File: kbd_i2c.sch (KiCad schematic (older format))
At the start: 78 parts, among them J1 Conn_01x04, SW1 MX_1u, SW10 MX_1u, SW11 MX_1u, SW12 MX_1u, SW13 MX_1u, SW14 MX_1u, SW15 MX_1u, SW16 MX_1u, SW17 MX_1u, SW18 MX_1u, SW19 MX_1u, SW2 MX_1u, SW20 MX_1u, SW21 MX_1u, SW22 MX_1u, SW23 MX_1u, SW24 MX_1u, SW25 SW_Push, SW26 SW_Push, SW27 SW_Push, SW28 SW_Push, SW3 MX_1u, SW4 MX_1u, SW5 MX_1u, SW6 MX_1u, SW7 MX_1u, SW8 MX_1u, SW9 MX_1u, U1 MCP23017_SO

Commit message: correction empreinte et routage; utilisation empreinte cherry mx led
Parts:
- removed D25, D28, D29, D32: LED, LED_THT:LED_D5.0mm, symbol Device:LED
- removed SW11, SW17, SW24, SW5: MX_1u, Button_Switch_Keyboard:SW_Cherry_MX_1.00u_PCB, symbol Switch:SW_Push
- added SW11, SW17, SW23, SW5: SW_Push_LED, Chimere:SW_MX_LED, symbol Switch:SW_Push_LED
- renumbered D20 to D19, D21 to D20, D22 to D21, D23 to D22, D24 to D23, D19 to D24, SW20 to SW19, SW21 to SW20, SW22 to SW21, SW23 to SW22, SW19 to SW24
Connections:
- wire segments 205 -> 201
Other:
- moved on the sheet: D1, D10, D11, D12, D13, D14, D15, D16, D17, D18, D19, D2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

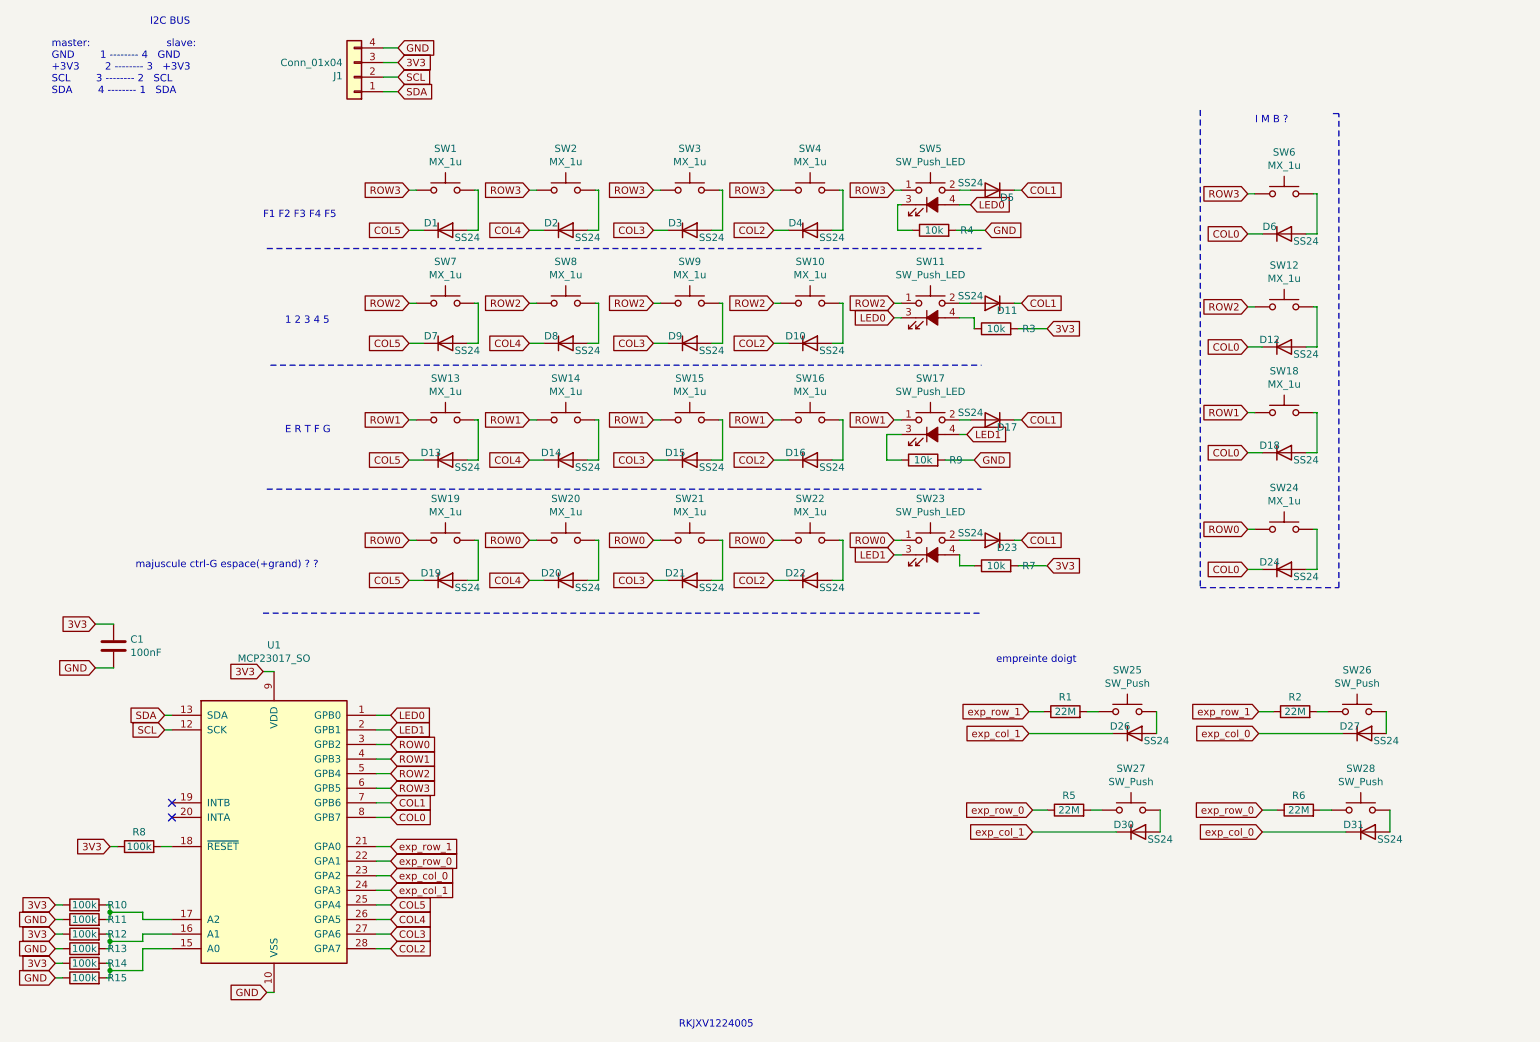
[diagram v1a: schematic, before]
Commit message: schema + routage
- redistribution des touches
- ajout 5ways switch
- supprimé les empreintes pcb de touches résistives
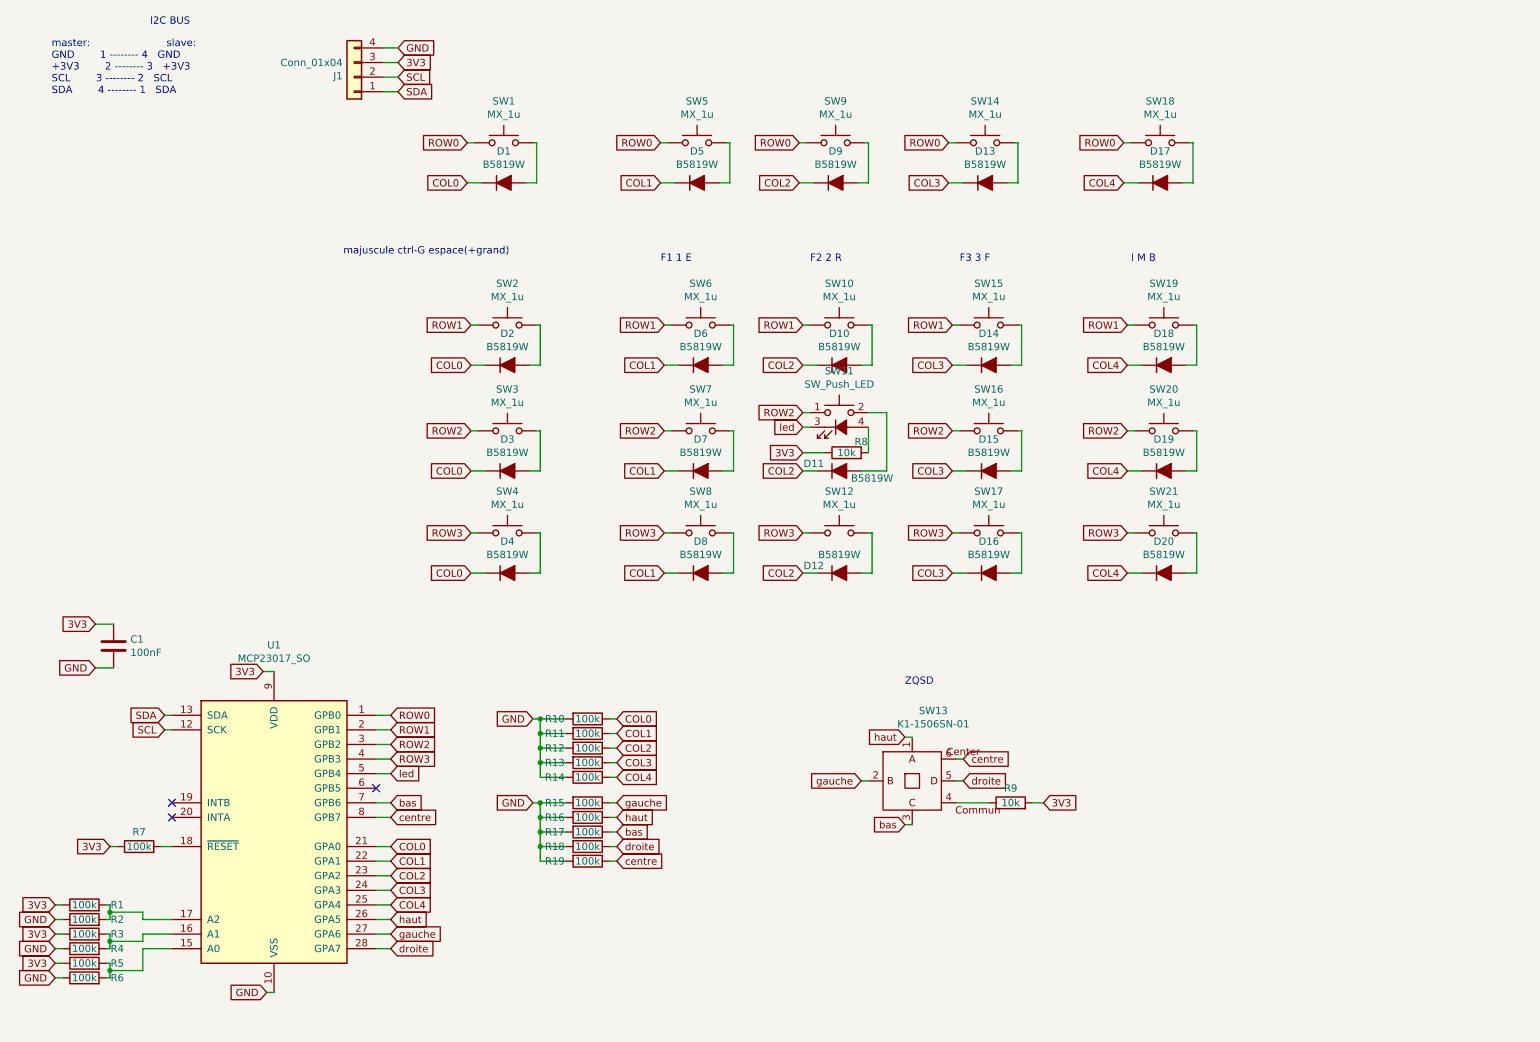
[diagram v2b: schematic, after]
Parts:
- removed D1, D10, D11, D12, D13, D14, D15, D16, D17, D18, D19, D2, D20, D21, D22, D23, D24, D26, D27, D3, D30, D31, D4, D5, D6, D7, D8, D9: SS24, Diode_SMD:D_SMA, symbol Device:D
- removed R1, R2, R5, R6: 22M, Resistor_SMD:R_0603_1608Metric_Pad1.05x0.95mm_HandSolder, symbol Device:R
- removed R3, R4, R7: 10k, Resistor_SMD:R_0603_1608Metric_Pad1.05x0.95mm_HandSolder, symbol Device:R
- removed SW13, SW2, SW22, SW24, SW3, SW4: MX_1u, Button_Switch_Keyboard:SW_Cherry_MX_1.00u_PCB, symbol Switch:SW_Push
- removed SW17, SW23, SW5: SW_Push_LED, Chimere:SW_MX_LED, symbol Switch:SW_Push_LED
- removed SW25, SW26, SW27, SW28: SW_Push, Chimere:doigt_sw, symbol Switch:SW_Push
- added D1, D10, D11, D12, D13, D14, D15, D16, D17, D18, D19, D2, D20, D3, D4, D5, D6, D7, D8, D9: B5819W, Diode_SMD:D_SOD-123, symbol Device:D_ALT
- added R10, R11, R12, R13, R14, R15, R16, R17, R18, R19: 100k, Resistor_SMD:R_0603_1608Metric, symbol Device:R
- added R8: 10k, Resistor_SMD:R_0603_1608Metric, symbol Device:R
- added SW12, SW17, SW18, SW5, SW6: MX_1u, Button_Switch_Keyboard:SW_Cherry_MX_1.00u_PCB, symbol Switch:SW_Push
- added SW13: K1-1506SN-01, Chimere:K1-1506SN-01, symbol Chimere:K1-1506SN-01
- C1: footprint Capacitor_SMD:C_0603_1608Metric_Pad1.05x0.95mm_HandSolder -> Capacitor_SMD:C_0603_1608Metric
- R1: renamed from R10; footprint Resistor_SMD:R_0603_1608Metric_Pad1.05x0.95mm_HandSolder -> Resistor_SMD:R_0603_1608Metric
- R2: renamed from R11; footprint Resistor_SMD:R_0603_1608Metric_Pad1.05x0.95mm_HandSolder -> Resistor_SMD:R_0603_1608Metric
- R3: renamed from R12; footprint Resistor_SMD:R_0603_1608Metric_Pad1.05x0.95mm_HandSolder -> Resistor_SMD:R_0603_1608Metric
- R4: renamed from R13; footprint Resistor_SMD:R_0603_1608Metric_Pad1.05x0.95mm_HandSolder -> Resistor_SMD:R_0603_1608Metric
- R5: renamed from R14; footprint Resistor_SMD:R_0603_1608Metric_Pad1.05x0.95mm_HandSolder -> Resistor_SMD:R_0603_1608Metric
- R6: renamed from R15; footprint Resistor_SMD:R_0603_1608Metric_Pad1.05x0.95mm_HandSolder -> Resistor_SMD:R_0603_1608Metric
- R7: renamed from R8; footprint Resistor_SMD:R_0603_1608Metric_Pad1.05x0.95mm_HandSolder -> Resistor_SMD:R_0603_1608Metric
- R9: footprint Resistor_SMD:R_0603_1608Metric_Pad1.05x0.95mm_HandSolder -> Resistor_SMD:R_0603_1608Metric
- renumbered SW12 to SW2, SW18 to SW3, SW6 to SW4
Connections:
- net COL5 is gone; now on net COL4: U1.25 (GPA4)
- net LED1 is gone; now on net ROW1: U1.2 (GPB1)
- net exp_col_0 is gone; now on net COL2: U1.23 (GPA2)
- net exp_col_1 is gone; now on net COL3: U1.24 (GPA3)
- net exp_row_0 is gone; now on net COL1: U1.22 (GPA1)
- net exp_row_1 is gone; now on net COL0: U1.21 (GPA0)
- net 3V3: now also R9.2, R8.1
- net COL0: now also D1.1 (K), D2.1 (K), D3.1 (K), D4.1 (K), R10.1; no longer U1.8 (GPB7)
- net COL1: now also D5.1 (K), D6.1 (K), D7.1 (K), D8.1 (K), R11.1; no longer U1.7 (GPB6)
- net COL2: now also D10.1 (K), D11.1 (K), D12.1 (K), D9.1 (K), R12.1; no longer U1.28 (GPA7)
- net COL3: now also D13.1 (K), D14.1 (K), D15.1 (K), D16.1 (K), R13.1; no longer U1.27 (GPA6)
- net COL4: now also D17.1 (K), D18.1 (K), D19.1 (K), D20.1 (K), R14.1; no longer U1.26 (GPA5)
- net GND: now also R10.2, R11.2, R12.2, R13.2, R14.2, R15.2, R16.2, R17.2, R18.2, R19.2; no longer R9.2
- net ROW0: now also SW1.1, SW14.1, SW9.1, U1.1 (GPB0), SW18.1, SW5.1; no longer SW19.1, SW20.1, SW21.1, U1.3 (GPB2)
- net ROW1: now also SW10.1, SW19.1, SW2.1, SW6.1; no longer SW14.1, SW16.1, SW3.1, U1.4 (GPB3)
- net ROW2: now also SW16.1, SW20.1, SW3.1, U1.3 (GPB2); no longer SW10.1, SW2.1, SW8.1, SW9.1, U1.5 (GPB4)
- net ROW3: now also SW21.1, SW8.1, U1.4 (GPB3), SW12.1, SW17.1; no longer SW1.1, U1.6 (GPB5)
- net at SW1.2: now also D1.2 (A)
- net at SW4.2: now also D4.2 (A)
- net at SW7.2: now also D7.2 (A)
- net at SW8.2: now also D8.2 (A)
- net at SW9.2: now also D9.2 (A)
- net at SW10.2: now also D10.2 (A)
- net at SW2.2: now also D2.2 (A)
- net at SW14.2: now also D13.2 (A)
- net at SW15.2: now also D14.2 (A)
- net at SW16.2: now also D15.2 (A)
- net at SW3.2: now also D3.2 (A)
- net at SW19.2: now also D18.2 (A)
- net at SW20.2: now also D19.2 (A)
- net at SW21.2: now also D20.2 (A)
- net at SW11.4 (A): now also R8.2
- net at R9.1: now also SW13.4
- net at SW11.2: now also D11.2 (A)
- net LED0 renamed led
- net led: now also U1.5 (GPB4); no longer U1.1 (GPB0)
- new net: D6.2 (A), SW6.2
- new net: D12.2 (A), SW12.2
- new net: D16.2 (A), SW17.2
- new net: D5.2 (A), SW5.2
- new net: D17.2 (A), SW18.2
- new net bas: R17.1, SW13.3, U1.7 (GPB6)
- new net centre: R19.1, SW13.6, U1.8 (GPB7)
- new net droite: R18.1, SW13.5, U1.28 (GPA7)
- new net gauche: R15.1, SW13.2, U1.27 (GPA6)
- new net haut: R16.1, SW13.1, U1.26 (GPA5)
- no-connect marks 2 -> 3
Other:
- note added: "F1 1 E"
- note added: "F2 2 R"
- note added: "F3 3 F"
- note added: "I M B"
- note added: "ZQSD"
- note added: "majuscule ctrl-G espace(+grand)"
- note removed: "1 2 3 4 5"
- note removed: "E R T F G"
- note removed: "F1 F2 F3 F4 F5"
- note removed: "I M B ?"
- note removed: "RKJXV1224005"
- note removed: "empreinte doigt"
- note removed: "majuscule ctrl-G espace(+grand) ? ?"
- moved on the sheet: SW2, SW3, SW4

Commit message: correction schema et routage
changement symbole et empreinte de arduino micro socket
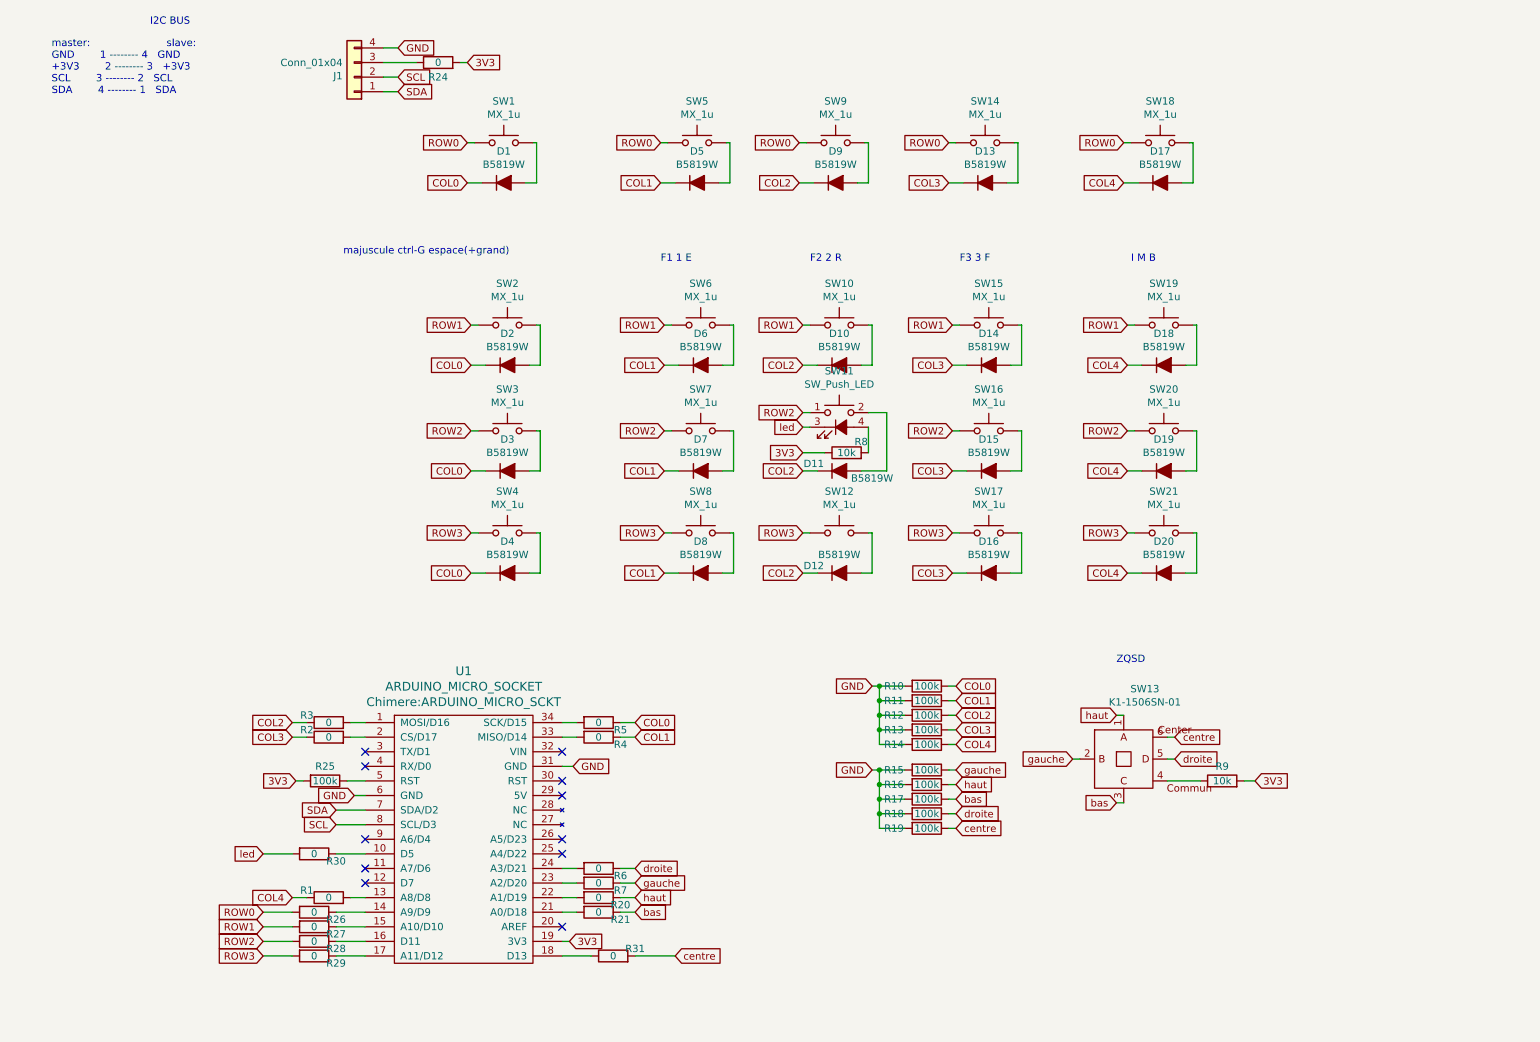
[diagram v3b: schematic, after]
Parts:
- removed C1: 100nF, Capacitor_SMD:C_0603_1608Metric, symbol Device:C
- removed U1: MCP23017_SO, Package_SO:SOIC-28W_7.5x17.9mm_P1.27mm, symbol Interface_Expansion:MCP23017_SO
- added R20, R21, R24, R26, R27, R28, R29, R30, R31: 0, Resistor_SMD:R_0603_1608Metric, symbol Device:R
- added R25: 100k, Resistor_SMD:R_0603_1608Metric, symbol Device:R
- added U1: ARDUINO_MICRO_SOCKET, Chimere:ARDUINO_MICRO_SCKT, symbol Chimere:ARDUINO_MICRO_SOCKET
- J1: footprint Connector_JST:JST_XH_S4B-XH-A_1x04_P2.50mm_Horizontal -> Connector_JST:JST_XH_B4B-XH-A_1x04_P2.50mm_Vertical
- R1, R2, R3, R4, R5, R6, R7: value 100k -> 0
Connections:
- net 3V3: now also R24.2, R25.2, U1.19 (3V3); no longer J1.3 (Pin_3), R1.1, R3.1, R5.1, R7.1
- net COL0: now also R5.1
- net COL1: now also R4.1
- net COL2: now also R3.1
- net COL3: now also R2.1
- net COL4: now also R1.1
- net GND: now also U1.31 (GND), U1.6 (GND); no longer R2.1, R4.1, R6.1
- net ROW0: now also R26.2
- net ROW1: now also R27.2
- net ROW2: now also R28.2
- net ROW3: now also R29.2
- net SCL: now also U1.8 (SCL/D3)
- net SDA: now also U1.7 (SDA/D2)
- net bas: now also R21.1
- net centre: now also R31.2
- net droite: now also R6.1
- net gauche: now also R7.1
- net haut: now also R20.1
- net led: now also R30.2
- net at R7.2: now also U1.23 (A2/D20)
- net at R5.2: now also U1.34 (SCK/D15); no longer R6.2
- net at R3.2: now also U1.1 (MOSI/D16); no longer R4.2
- net at R1.2: now also U1.13 (A8/D8); no longer R2.2
- new net: J1.3 (Pin_3), R24.1
- new net: R25.1, U1.5 (RST)
- new net: R2.2, U1.2 (CS/D17)
- new net: R4.2, U1.33 (MISO/D14)
- new net: R6.2, U1.24 (A3/D21)
- new net: R20.2, U1.22 (A1/D19)
- new net: R21.2, U1.21 (A0/D18)
- new net: R26.1, U1.14 (A9/D9)
- new net: R27.1, U1.15 (A10/D10)
- new net: R28.1, U1.16 (D11)
- new net: R29.1, U1.17 (A11/D12)
- new net: R30.1, U1.10 (D5)
- new net: R31.1, U1.18 (D13)
- no-connect marks 3 -> 11
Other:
- moved on the sheet: R10, R11, R12, R13, R14, R15, R16, R17, R18, R19, R9, SW13

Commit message: maj split librairies
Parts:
- SW11: footprint Chimere:SW_MX_LED -> Chimere_comps:SW_MX_LED
- SW13: footprint Chimere:K1-1506SN-01 -> Chimere_comps:K1-1506SN-01; symbol Chimere:K1-1506SN-01 -> Chimere_comps:K1-1506SN-01
- U1: footprint Chimere:ARDUINO_MICRO_SCKT -> Chimere_comps:ARDUINO_MICRO_SCKT; symbol Chimere:ARDUINO_MICRO_SOCKET -> Chimere_comps:ARDUINO_MICRO_SOCKET
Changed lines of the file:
@@
 $EndComp
 $Comp
-L Chimere:K1-1506SN-01 SW13
+L Chimere_comps:K1-1506SN-01 SW13
 U 1 1 60DCEFD1
 P 8200 5700
+AR Path="/60DCEFD1" Ref="SW13"  Part="1"
+AR Path="/6072E958/60DCEFD1" Ref="SW13"  Part="1"
 F 0 "SW13" H 8345 6181 50  0000 C CNN
 F 1 "K1-1506SN-01" H 8345 6090 50  0000 C CNN
-F 2 "Chimere:K1-1506SN-01" H 8200 5700 50  0001 C CNN
+F 2 "Chimere_comps:K1-1506SN-01" H 8200 5700 50  0001 C CNN
 F 3 "C145910" H 8200 5700 50  0001 C CNN
 	1    8200 5700
@@
 F 0 "SW11" H 6250 3810 50  0000 C CNN
 F 1 "SW_Push_LED" H 6250 3719 50  0000 C CNN
-F 2 "Chimere:SW_MX_LED" H 6250 3725 50  0001 C CNN
+F 2 "Chimere_comps:SW_MX_LED" H 6250 3725 50  0001 C CNN
 F 3 "~" H 6250 3725 50  0001 C CNN
 	1    6250 3425
@@
 NoConn ~ 3000 6550
 $Comp
-L Chimere:ARDUINO_MICRO_SOCKET U1
+L Chimere_comps:ARDUINO_MICRO_SOCKET U1
 U 1 1 60F2970B
 P 3200 5400
+AR Path="/60F2970B" Ref="U1"  Part="1"
+AR Path="/6072E958/60F2970B" Ref="U1"  Part="1"
 F 0 "U1" V 2897 5875 60  0000 C CNN
 F 1 "ARDUINO_MICRO_SOCKET" V 3003 5875 60  0000 C CNN
-F 2 "Chimere:ARDUINO_MICRO_SCKT" V 3109 5875 60  0000 C CNN
+F 2 "Chimere_comps:ARDUINO_MICRO_SCKT" V 3109 5875 60  0000 C CNN
 F 3 "" H 3600 5350 60  0000 C CNN
 	1    3200 5400
